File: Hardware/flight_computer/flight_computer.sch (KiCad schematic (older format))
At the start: 22 parts

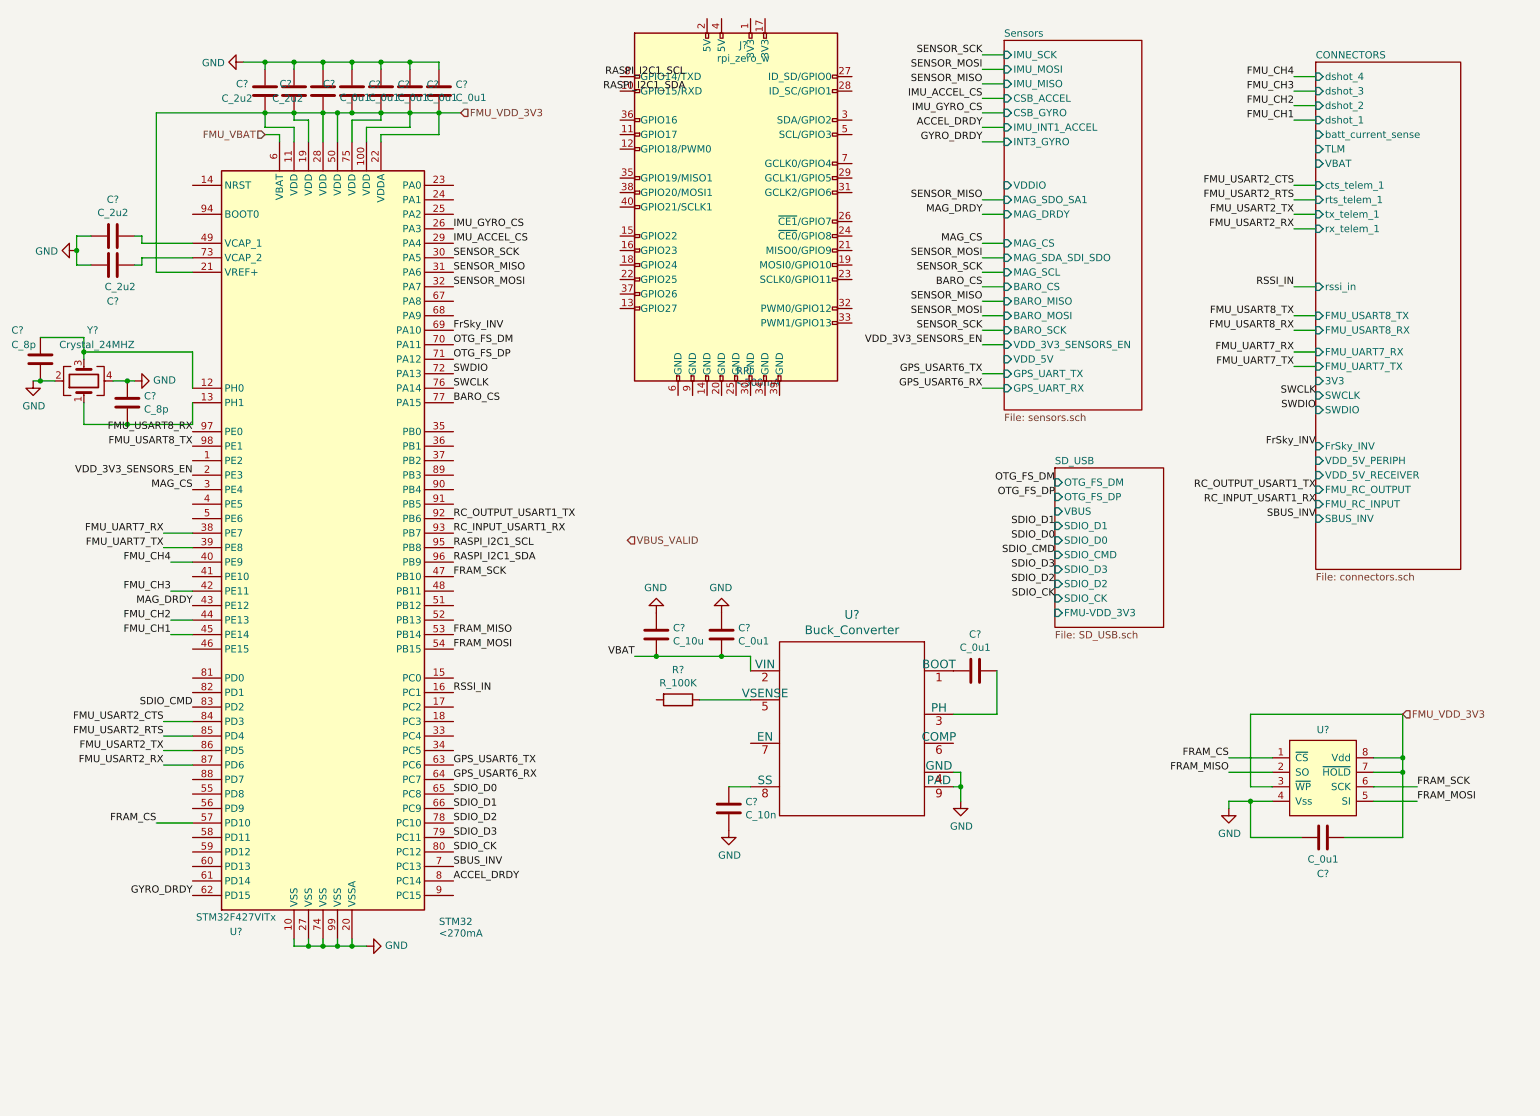
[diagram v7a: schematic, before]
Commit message: Adds in regulators and filters
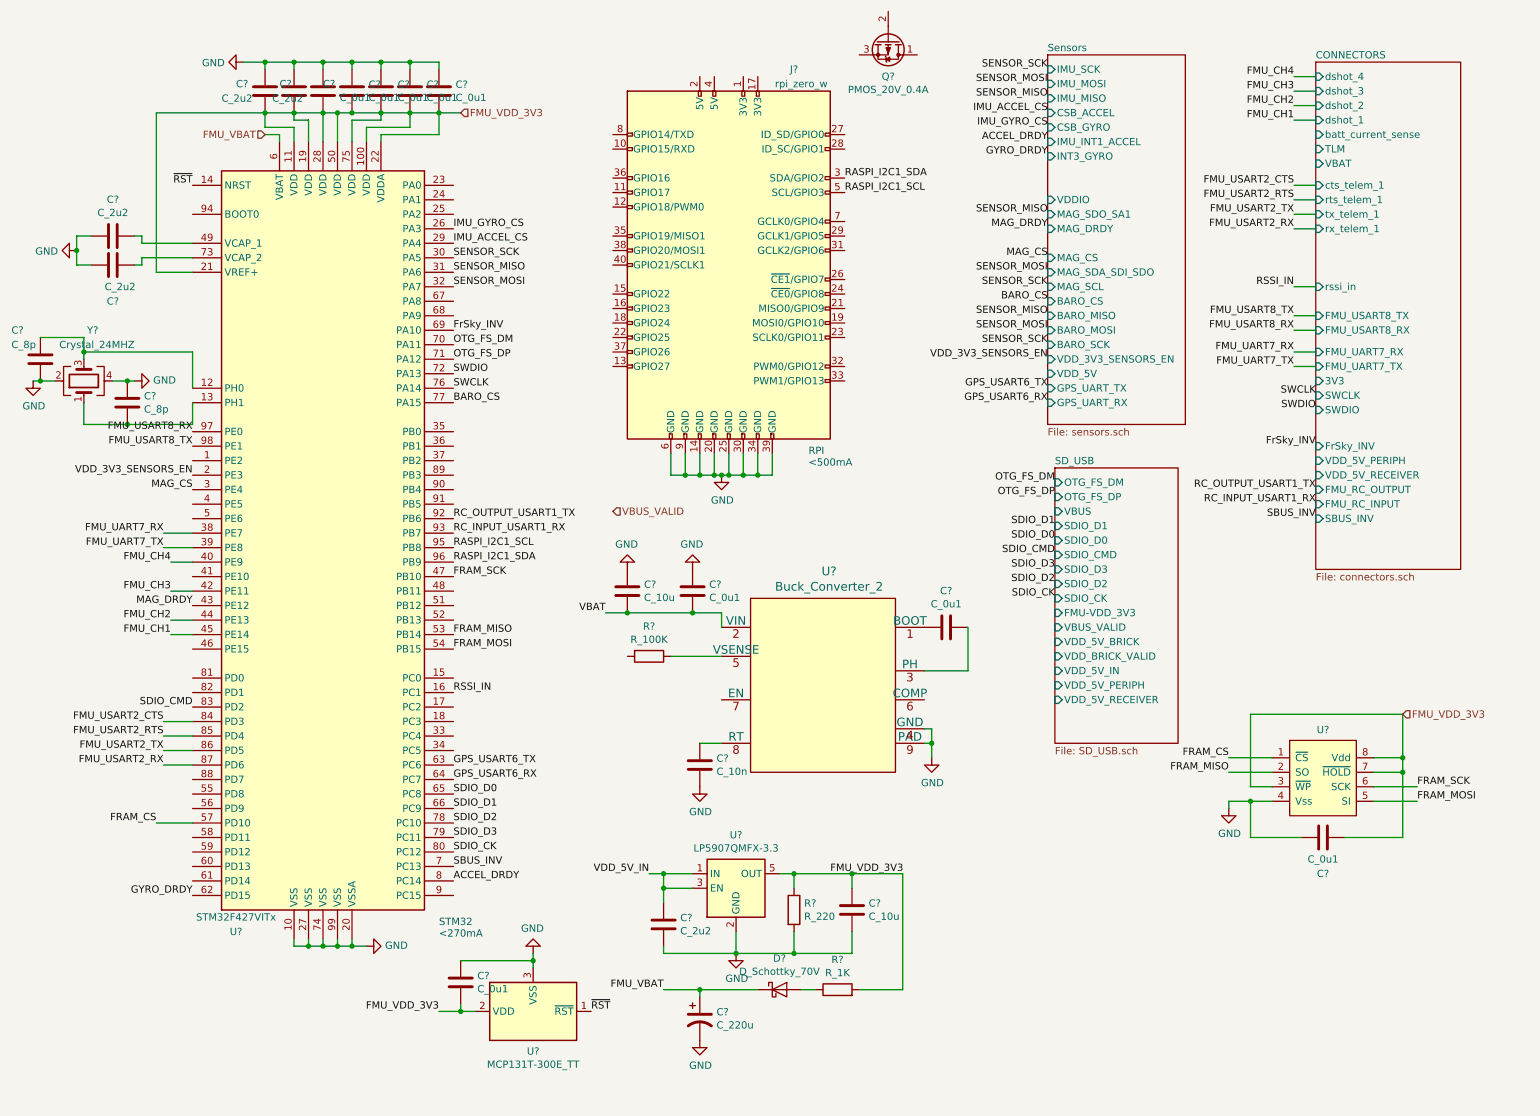
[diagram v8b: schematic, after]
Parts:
- removed U?: Buck_Converter, drone_footprints:TPS54336ADDAR, symbol openDrone_parts:Buck_Converter
- added C?: C_2u2, Capacitors_SMD:C_0805, symbol openDrone_parts:C_2u2
- added C?: C_10u, Capacitors_SMD:C_0805, symbol openDrone_parts:C_10u
- added C?: C_220u, drone_footprints:UWT0G221MCL6GS, symbol openDrone_parts:C_220u
- added C?: C_0u1, Capacitors_SMD:C_0805, symbol openDrone_parts:C_0u1
- added D?: D_Schottky_70V, Diodes_SMD:D_SOD-523, symbol openDrone_parts:D_Schottky_70V
- added Q?: PMOS_20V_0.4A, TO_SOT_Packages_SMD:SOT-323_SC-70, symbol openDrone_parts:PMOS_20V_0.4A
- added R?: R_220, Resistors_SMD:R_0805, symbol openDrone_parts:R_220
- added R?: R_1K, Resistors_SMD:R_0805, symbol openDrone_parts:R_1K
- added U?: Buck_Converter_2, drone_footprints:TPS54335ADDA, symbol openDrone_parts:Buck_Converter_2
- added U?: LP5907QMFX-3.3, TO_SOT_Packages_SMD:SOT-23-5, symbol openDrone_parts:LP5907QMFX-3.3
- added U?: MCP131T-300E_TT, Package_TO_SOT_SMD:SOT-23, symbol openDrone_parts:MCP131T-300E_TT
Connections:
- net FMU_VBAT: now also C?.1, D?.1 (K)
- net FMU_VDD_3V3: now also C?.1, C?.2, R?.1, R?.2, U?.2 (VDD), U?.5 (OUT)
- net GND: now also J?.14 (GND), J?.20 (GND), J?.25 (GND), J?.30 (GND), J?.34 (GND), J?.39 (GND), J?.6 (GND), J?.9 (GND), C?.1, C?.2, C?.2, C?.2, R?.2, U?.2 (GND), U?.3 (VSS), U?.4 (GND), U?.9 (PAD)
- net RASPI_I2C1_SCL: now also J?.5 (SCL/GPIO3)
- net RASPI_I2C1_SDA: now also J?.3 (SDA/GPIO2)
- net VBAT: now also U?.2 (VIN)
- net ~RST: now reaches U?.14 (NRST)
- net ~RST: now also U?.1 (~RST)
- net at C?.2: now also U?.1 (BOOT)
- net at C?.1: now also U?.3 (PH)
- net at R?.1: now also U?.5 (VSENSE)
- net at C?.1: now also U?.8 (RT)
- new net: D?.2 (A), R?.1
- new net VDD_5V_IN: C?.1, U?.1 (IN), U?.3 (EN)
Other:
- moved on the sheet: C?, J?, R?
